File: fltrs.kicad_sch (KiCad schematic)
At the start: 25 parts, among them U4 MCP6002, U5 MCP6002, U6 MCP4551

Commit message: WIP filters
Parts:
- removed C14, C21: 10n, Capacitor_SMD:C_0603_1608Metric, symbol Device:C
- removed C19: 680p, Capacitor_SMD:C_0603_1608Metric, symbol Device:C
- removed C23: 1u, Capacitor_SMD:C_0603_1608Metric, symbol Device:C
- removed R11: 39k, Resistor_SMD:R_0603_1608Metric, symbol Device:R_Small
- removed R14: 3k9, Resistor_SMD:R_0603_1608Metric, symbol Device:R_Small
- removed R16: 2k2, Resistor_SMD:R_0603_1608Metric, symbol Device:R_Small
- removed R9: 3k3, Resistor_SMD:R_0603_1608Metric, symbol Device:R_Small
- removed RV1: 50k, symbol Device:R_Potentiometer
- removed RV2: 50k, Potentiometer_SMD:Potentiometer_Bourns_3224J_Horizontal, symbol Device:R_Potentiometer
- removed U6 (x2): MCP4551, Package_SO:MSOP-8_3x3mm_P0.65mm, symbol micro17:MCP4551
- added C13, C20: 10n, Capacitor_SMD:C_0603_1608Metric, symbol Device:C_Small
- added C17, C24: 100n, Capacitor_SMD:C_0603_1608Metric, symbol Device:C_Small
- added C18: 1n5, Capacitor_SMD:C_0603_1608Metric, symbol Device:C_Small
- added C22: 220n, Capacitor_SMD:C_0603_1608Metric, symbol Device:C_Small
- added C25 (x2): 680p, Capacitor_SMD:C_0805_2012Metric, symbol Device:C_Small
- added C28, C33: 10n, symbol Device:C_Small
- added C30: 22u, symbol Device:C_Polarized_Small
- added R10: 13k, Resistor_SMD:R_0603_1608Metric, symbol Device:R_Small
- added R13: 7k5, Resistor_SMD:R_0603_1608Metric, symbol Device:R_Small
- added R15: 39k, Resistor_SMD:R_0603_1608Metric, symbol Device:R_Small
- added R15: 3k9, Resistor_SMD:R_0603_1608Metric, symbol Device:R_Small
- added R17: 10k, symbol Device:R_Small
- added R19: 3k9, symbol Device:R_Small
- added R8: 4k3, Resistor_SMD:R_0603_1608Metric, symbol Device:R_Small
- added U4: MCP6002, Package_DFN_QFN:DFN-8-1EP_3x2mm_P0.5mm_EP1.75x1.45mm, symbol Amplifier_Operational:MCP6002-xMC
- added U8: MCP4451-503-ST, Package_SO:TSSOP-20_4.4x6.5mm_P0.65mm, symbol Potentiometer_Digital:MCP4451-xxxx-ST
- C13: value 4n7 -> 10n; symbol Device:C -> Device:C_Small
- C17, C24: symbol Device:C -> Device:C_Small
- C18: value 220p -> 1n5; symbol Device:C -> Device:C_Small
- C20: value 1n5 -> 10n; symbol Device:C -> Device:C_Small
- C22: value 1u -> 220n; symbol Device:C -> Device:C_Small
- C25: value 22u/25V -> 10n; symbol Device:C -> Device:C_Small
- R10: value 130k -> 13k
- R13: value 36k -> 7k5
- R15: value 10k -> 3k3
- R8: value 9k1 -> 4k3
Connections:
- net +5V: now also C24.1, U4.8 (V+)
- net BASEBAND_OUT: now also U8.20 (P2A)
- net GND: now also C13.2, C17.2, C18.2, C24.2, C25.2, C25.2, U4.4 (V-), U4.9 (V-), U8.13 (P0B), U8.16 (A1), U8.18 (P2B), U8.4 (HVC/A0), U8.7 (VSS), U8.8 (P1B)
- net at U4.5 (+): now also C18.1, R13.2
- net at U4.6 (-), U4.7: now also C20.2, U8.10 (P1A)
- net at U5.1: now also R15.1, U5.2 (-); no longer R15.2
- net at U5.3 (+): now also U8.19 (P2W)
- net at C22.1: now also U8.12 (P0W)
- net at C20.2, U4.1, U4.2 (-): now also U8.11 (P0A)
- net at U5.5 (+): now also C25.1, R15.2
- net at U5.6 (-): now also U5.7, C28.2, C30.1
- net at C25.1: now also R15.2, R15.1
- new net: C20.1, R10.2, R13.1
- new net: C28.1, R15.1, R15.2
- new net: C22.1, U8.9 (P1W)
- new net: R17.2, U8.15 (~{RESET})
- new net: C25.1, R19.1, U4.5 (+)
- new net: C33.2, R19.2
- new net: C13.1, R10.1, R8.2
- new net +3V3: C17.1, R17.1, U8.17 (VDD)
- new net AUDIO_IN: R8.1
- new net AUDIO_IN_FILT: C22.2
- new net BASEBAND_IN_FILT: C33.1, U4.6 (-), U4.7
- new net BASEBAND_OUT_FILT: C30.2
- new net I2C_SCL: U8.5 (SCL)
- new net I2C_SDA: U8.6 (SDA)
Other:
- moved on the sheet: C13, C17, C18, C20, C22, C24, C25, R10, R13, R15, R8, U4A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

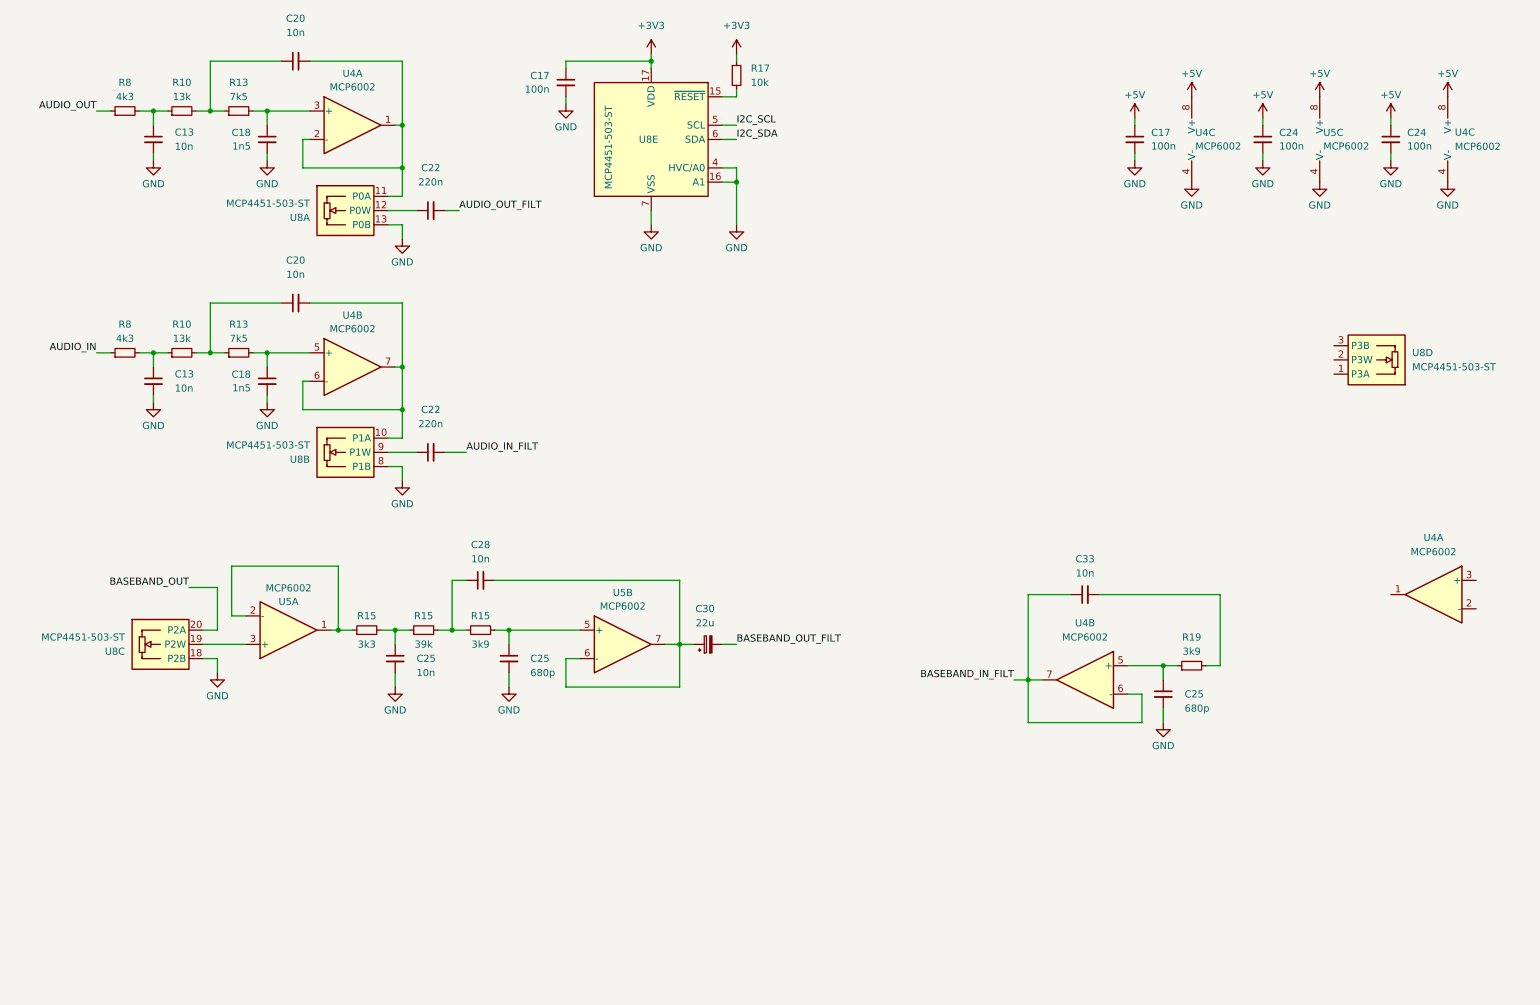
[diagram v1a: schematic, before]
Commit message: First Edits
Added J1 connector, finished filters and swapped µC to STM32G473
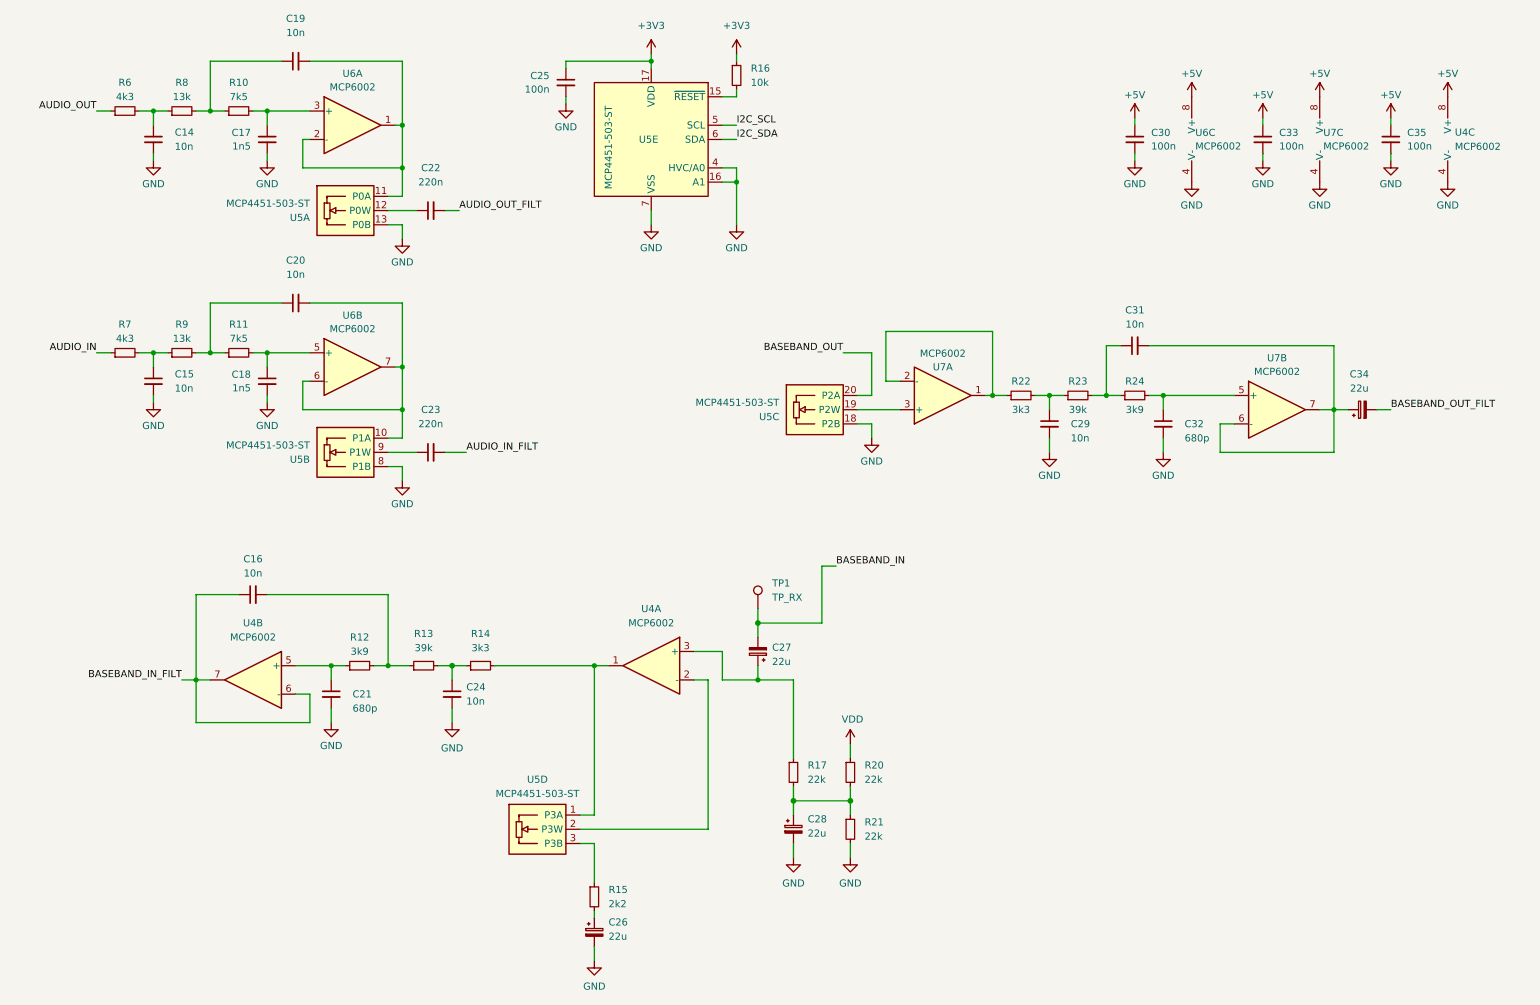
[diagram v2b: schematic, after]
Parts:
- added C24: 10n, Capacitor_SMD:C_0201_0603Metric, symbol Device:C_Small
- added C26, C27, C28: 22u, Capacitor_Tantalum_SMD:CP_EIA-3216-18_Kemet-A, symbol Device:C_Polarized_Small
- added R13: 39k, Resistor_SMD:R_0201_0603Metric, symbol Device:R_Small
- added R14: 3k3, Resistor_SMD:R_0201_0603Metric, symbol Device:R_Small
- added R15: 2k2, Resistor_SMD:R_0201_0603Metric, symbol Device:R_Small
- added R17, R20, R21: 22k, Resistor_SMD:R_0201_0603Metric, symbol Device:R_Small
- added TP1: TP_RX, TestPoint:TestPoint_Pad_D1.0mm, symbol Connector:TestPoint
- C14, C15: renamed from C13; footprint Capacitor_SMD:C_0603_1608Metric -> Capacitor_SMD:C_0201_0603Metric
- C16: renamed from C33; footprint (none) -> Capacitor_SMD:C_0201_0603Metric
- C17: renamed from C18; footprint Capacitor_SMD:C_0603_1608Metric -> Capacitor_SMD:C_0201_0603Metric
- C18, C20, C22: footprint Capacitor_SMD:C_0603_1608Metric -> Capacitor_SMD:C_0201_0603Metric
- C19: renamed from C20; footprint Capacitor_SMD:C_0603_1608Metric -> Capacitor_SMD:C_0201_0603Metric
- C23: renamed from C22; footprint Capacitor_SMD:C_0603_1608Metric -> Capacitor_SMD:C_0201_0603Metric
- C25, C30: renamed from C17; footprint Capacitor_SMD:C_0603_1608Metric -> Capacitor_SMD:C_0201_0603Metric
- C31: renamed from C28; footprint (none) -> Capacitor_SMD:C_0201_0603Metric
- C33, C35: renamed from C24; footprint Capacitor_SMD:C_0603_1608Metric -> Capacitor_SMD:C_0201_0603Metric
- C34: renamed from C30; footprint (none) -> Capacitor_Tantalum_SMD:CP_EIA-3216-18_Kemet-A
- R10, R11: renamed from R13; footprint Resistor_SMD:R_0603_1608Metric -> Resistor_SMD:R_0201_0603Metric
- R12: renamed from R19; footprint (none) -> Resistor_SMD:R_0201_0603Metric
- R16: renamed from R17; footprint (none) -> Resistor_SMD:R_0201_0603Metric
- R22, R23, R24: renamed from R15; footprint Resistor_SMD:R_0603_1608Metric -> Resistor_SMD:R_0201_0603Metric
- R6, R7: renamed from R8; footprint Resistor_SMD:R_0603_1608Metric -> Resistor_SMD:R_0201_0603Metric
- R8, R9: renamed from R10; footprint Resistor_SMD:R_0603_1608Metric -> Resistor_SMD:R_0201_0603Metric
- renumbered C25 to C21, C25 to C29, C25 to C32, U8 to U5, U4 to U6, U5 to U7
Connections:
- net GND: now also C24.2, C26.2, C28.2, R21.2
- net at C16.2, R12.2: now also R13.1
- net at U5.1 (P3A): now also U4.1, R14.2
- net at U5.2 (P3W): now also U4.2 (-)
- net at U5.3 (P3B): now also R15.1
- net at U4.3 (+): now also C27.1, R17.1
- new net: C26.1, R15.2
- new net: C24.1, R13.2, R14.1
- new net: C28.1, R17.2, R20.2, R21.1
- new net BASEBAND_IN: C27.2, TP1.1
- new net VDD: R20.1
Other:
- moved on the sheet: C16, C21, C29, C31, C32, C34, R12, R22, R23, R24, U4A, U4B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

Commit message: PCB routed, gerbers and ibom included
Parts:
- added R18, R19: 3k3, Resistor_SMD:R_0402_1005Metric, symbol Device:R_Small
- added TP2: TP_TX, TestPoint:TestPoint_Pad_D1.0mm, symbol Connector:TestPoint
- C14, C15, C16, C17, C18, C19, C20, C22, C23, C24, C25, C30, C31, C33, C35: footprint Capacitor_SMD:C_0201_0603Metric -> Capacitor_SMD:C_0402_1005Metric
- C21, C29, C32: footprint Capacitor_SMD:C_0805_2012Metric -> Capacitor_SMD:C_0402_1005Metric
- R10, R11, R12, R13, R14, R15, R16, R17, R20, R21, R22, R23, R6, R7, R8, R9: footprint Resistor_SMD:R_0201_0603Metric -> Resistor_SMD:R_0402_1005Metric
- R24: footprint Resistor_SMD:R_0201_0603Metric -> Resistor_SMD:R_0603_1608Metric
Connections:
- net VDD is gone; now on net +5V: R20.1
- net +3V3: now also R18.1, R19.1
- net BASEBAND_OUT_FILT: now also TP2.1
- net I2C_SCL: now also R18.2
- net I2C_SDA: now also R19.2
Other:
- moved on the sheet: C26, R15, U5D

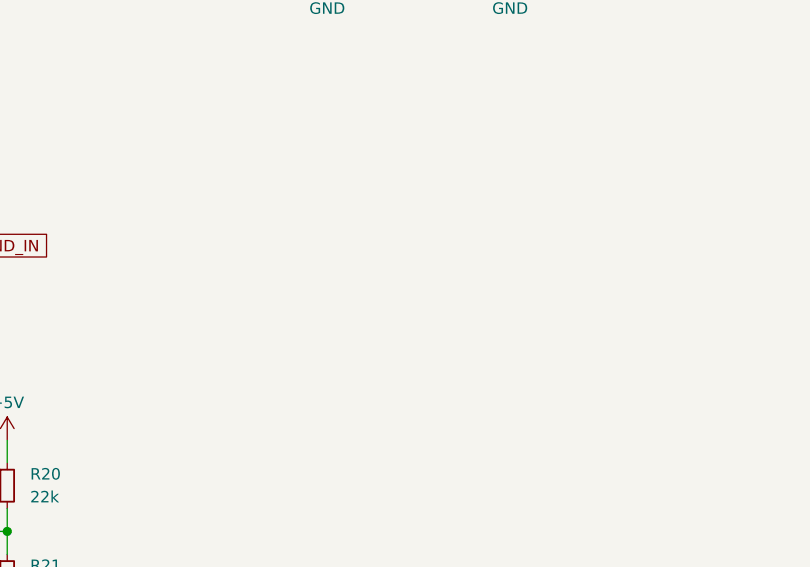
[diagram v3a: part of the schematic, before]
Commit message: Updates
GP relay added,
3v3 added to programming conn.
diode(dnp) added for motorola type internal bus.
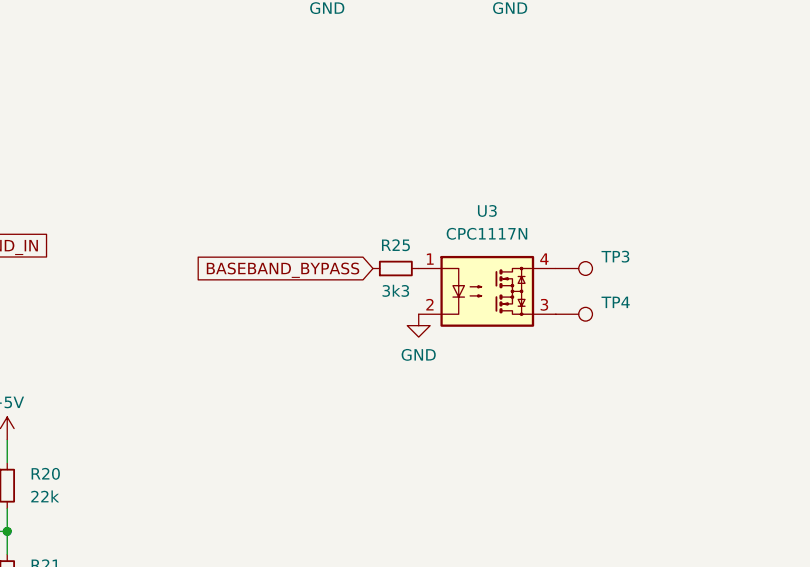
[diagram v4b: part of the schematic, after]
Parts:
- added R25: 3k3, Resistor_SMD:R_0402_1005Metric, symbol Device:R_Small
- added TP3, TP4: GP, TestPoint:TestPoint_Pad_D1.0mm, symbol Connector:TestPoint
- added U3: CPC1117N, Package_SO:SOP-4_3.8x4.1mm_P2.54mm, symbol Relay_SolidState:CPC1117N
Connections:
- net GND: now also U3.2
- new net: R25.2, U3.1
- new net: TP4.1, U3.3
- new net: TP3.1, U3.4
- new net BASEBAND_BYPASS: R25.1

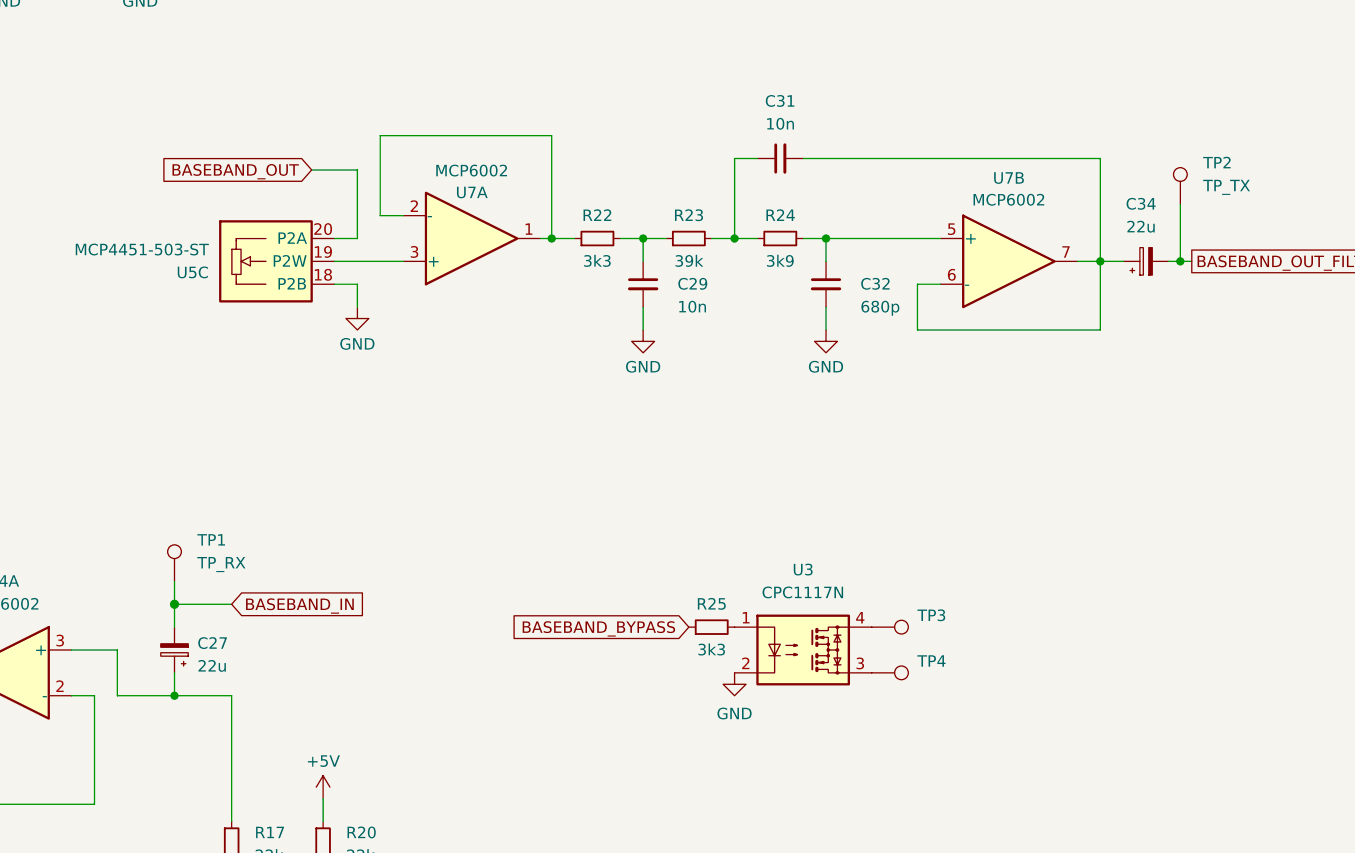
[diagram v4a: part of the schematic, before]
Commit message: LCSC part numbers included into schematics
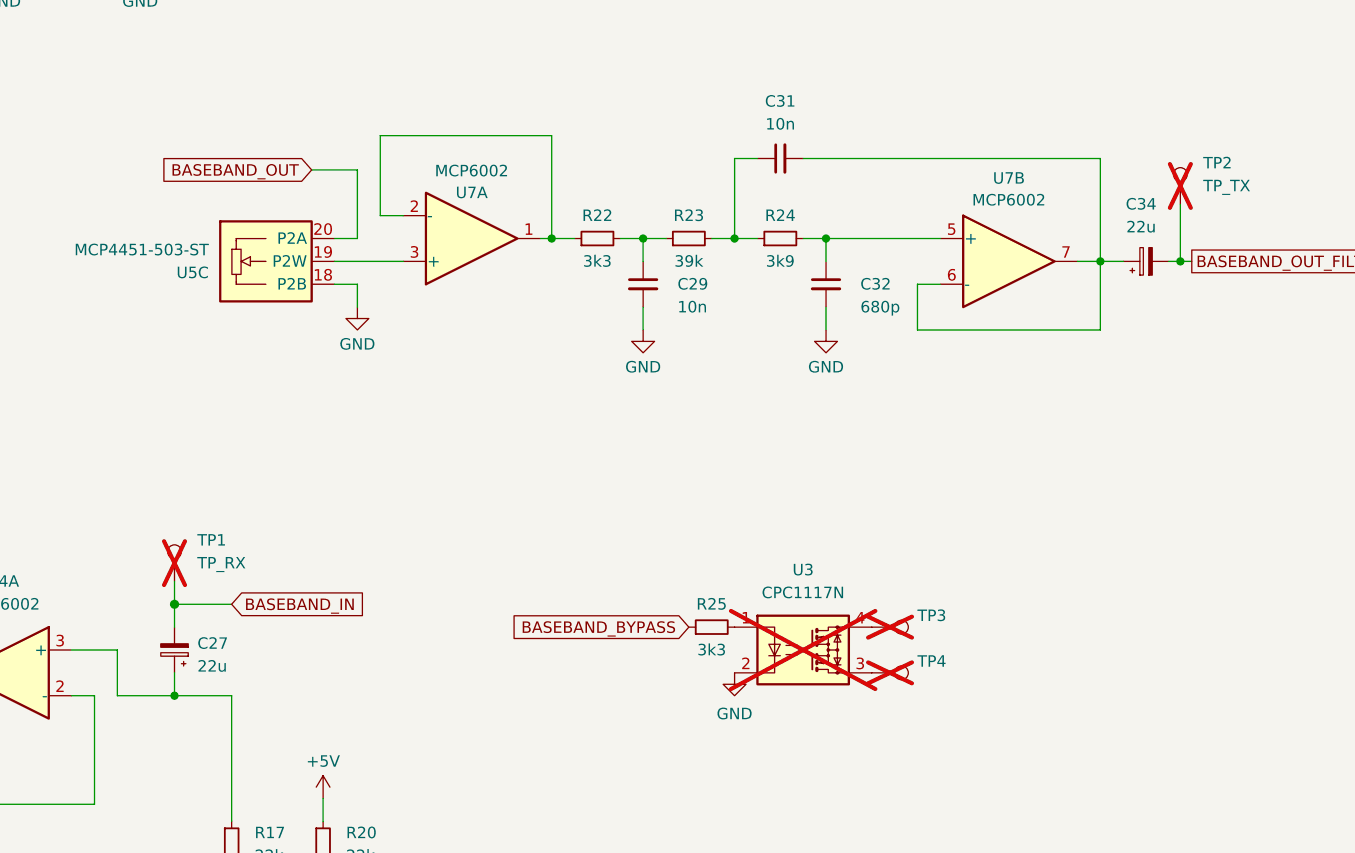
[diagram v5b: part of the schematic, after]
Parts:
- C14, C15, C16, C19, C20, C24, C29, C31: LCSC (none) -> C60133
- C17, C18: LCSC (none) -> C284989
- C21, C32: LCSC (none) -> C1541
- C22, C23: LCSC (none) -> C192432
- C25, C30, C33, C35: LCSC (none) -> C56392
- C26, C27, C28: LCSC (none) -> C118989; LCSC Part # C118989 -> (none)
- C34: LCSC (none) -> C118989
- R10, R11: LCSC (none) -> C2960875
- R12: LCSC (none) -> C3015806
- R13, R23: LCSC (none) -> C25783
- R14, R18, R19, R22, R25: LCSC (none) -> C25890
- R15: LCSC (none) -> C102890
- R16: LCSC (none) -> C102749
- R17, R20, R21: LCSC (none) -> C2909337
- R24: LCSC (none) -> C23018
- R6, R7: LCSC (none) -> C25899
- R8, R9: LCSC (none) -> C25754
- TP1, TP2, TP3, TP4, U3: now not fitted
- U4, U6, U7: LCSC (none) -> C623660
- U5: LCSC (none) -> C627257
